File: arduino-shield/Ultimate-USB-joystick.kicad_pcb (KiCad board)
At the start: 2 copper layers, 68.6 x 53.3 mm, 25 parts

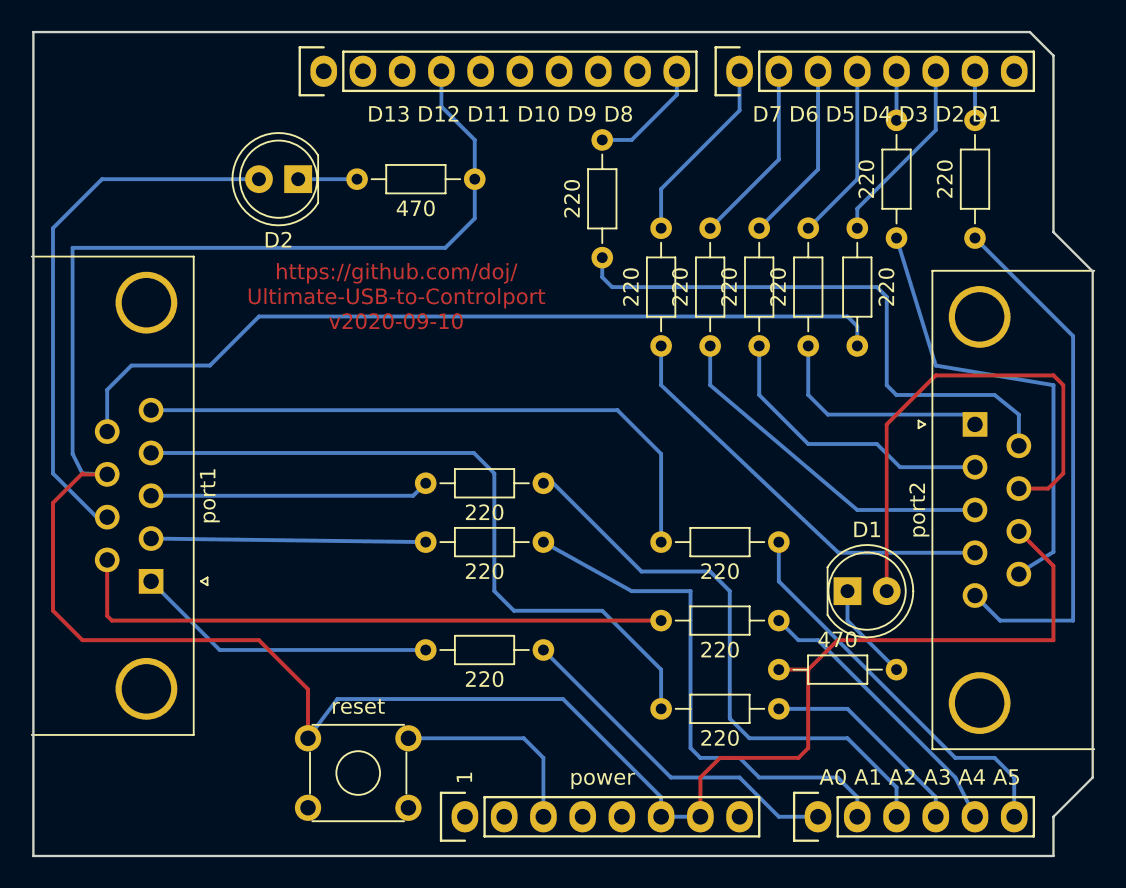
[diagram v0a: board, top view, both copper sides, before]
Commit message: increase R pad size, rename LED, fix reset switch
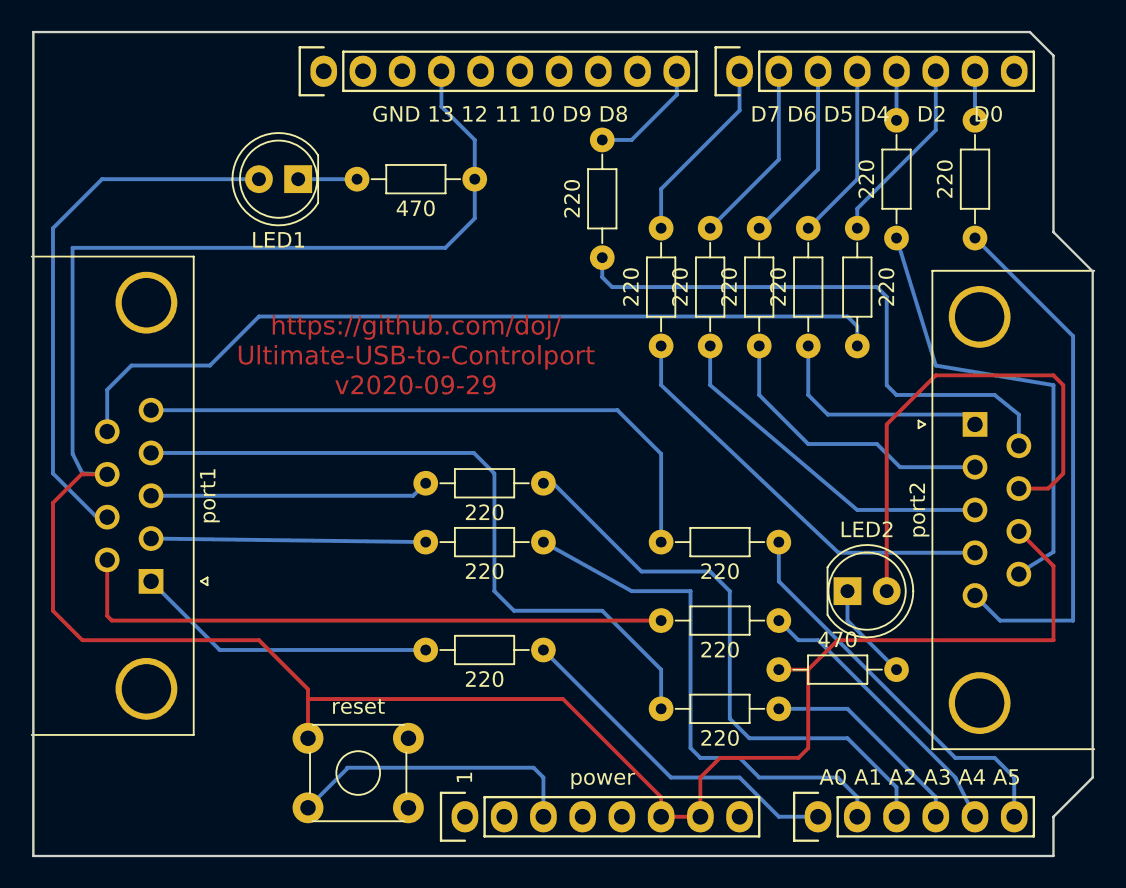
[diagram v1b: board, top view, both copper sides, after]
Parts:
-          GND 13 12 11 10 D9 D8: renamed from D13 D12 D11 D10 D9 D8
- D7 D6 D5 D4    D2    D0: renamed from D7 D6 D5 D4 D3 D2 D1
- renumbered D2 to LED1, D1 to LED2
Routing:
- net /Reset: track 13.1 -> 19.2 mm
- net GND: track 160.1 -> 158.8 mm
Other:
- board text added: "https://github.com/doj/ Ultimate-USB-to-Controlport v2020-09-29"
- board text removed: "https://github.com/doj/ Ultimate-USB-to-Controlport v2020-09-10"
